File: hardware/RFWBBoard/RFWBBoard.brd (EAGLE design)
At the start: 90 x 56 mm, 87 parts, among them IC1 24LC025ST, J1 CON-71742-2184-BOT, M1 MOUNT-HOLE3.3, M2 MOUNT-HOLE3.3, M3 MOUNT-HOLE3.3, M4 MOUNT-HOLE3.3, U1 MAX2830IPC-7351, U2 LDB212G4010C-001, U3 LDB212G4010C-001, U4 AD8132MSOP8, U5 AD8132MSOP8, U6 AD8132MSOP8, U7 AD8132MSOP8, X1 LTI-SASF54GT, X2 LTI-SASF54GT, X4 LTI-SASF54GT, X5 LTI-SASF54GT, X6 LTI-SASF54GT, X7 LTI-SASF54GT

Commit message: - Schematic updated - Info text updated on PCB back - 84 pin component changed in library
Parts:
- J1: value CON-71742-2184-BOT -> CON-71742-3003-BOT
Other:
- board text added: "Radio Front-End Board Rev A"
- board text removed: "Radio Front-End Board"
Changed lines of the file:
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@@
 <grid distance="1" unitdist="mm" unit="mm" style="dots" multiple="1" display="yes" altdistance="0.05" altunitdist="mm" altunit="mm"/>
 <layers>
-<layer number="1" name="Top" color="4" fill="1" visible="no" active="yes"/>
+<layer number="1" name="Top" color="4" fill="1" visible="yes" active="yes"/>
 <layer number="2" name="Route2" color="14" fill="1" visible="no" active="yes"/>
 <layer number="3" name="Route3" color="4" fill="1" visible="no" active="yes"/>
 <layer number="14" name="Route14" color="1" fill="6" visible="no" active="no"/>
 <layer number="15" name="Route15" color="4" fill="6" visible="no" active="no"/>
-<layer number="16" name="Bottom" color="14" fill="1" visible="no" active="yes"/>
+<layer number="16" name="Bottom" color="14" fill="1" visible="yes" active="yes"/>
 <layer number="17" name="Pads" color="2" fill="1" visible="yes" active="yes"/>
-<layer number="18" name="Vias" color="2" fill="1" visible="no" active="yes"/>
+<layer number="18" name="Vias" color="2" fill="1" visible="yes" active="yes"/>
 <layer number="19" name="Unrouted" color="6" fill="1" visible="yes" active="yes"/>
 <layer number="20" name="Dimension" color="15" fill="1" visible="yes" active="yes"/>
@@
 <wire x1="70" y1="19" x2="70" y2="36" width="0.2032" layer="22"/>
 <wire x1="70" y1="36" x2="20" y2="36" width="0.2032" layer="22"/>
-<text x="61" y="33" size="1.778" layer="22" font="vector" rot="MR0">Radio Front-End Board</text>
+<text x="66" y="33" size="1.778" layer="22" font="vector" rot="MR0">Radio Front-End Board Rev A</text>
 <text x="69" y="30" size="1.27" layer="22" font="vector" rot="MR0">7.5-18 MHz wide 2.4-2.5 GHz/Baseband module</text>
 <text x="57.75" y="27.75" size="1.27" layer="22" font="vector" rot="MR0">for the Marmote platform</text>
@@
 <element name="M3" library="RFWBBoard" package="3,3" value="MOUNT-HOLE3.3" x="5" y="5" locked="yes"/>
 <element name="M4" library="RFWBBoard" package="3,3" value="MOUNT-HOLE3.3" x="85" y="5" locked="yes"/>
-<element name="J1" library="RFWBBoard" package="71742-3003-BOT" value="CON-71742-2184-BOT" x="45" y="7" smashed="yes" rot="MR180">
-<attribute name="DIGI-KEY#" value="WM3499CT-ND" x="45" y="7" size="1.778" layer="28" rot="MR180" display="off"/>
-<attribute name="MATED-STACKING-HEIGHT" value="13mm, 15mm" x="45" y="7" size="1.778" layer="28" rot="MR180" display="off"/>
-<attribute name="MF" value="Molex" x="45" y="7" size="1.778" layer="28" rot="MR180" display="off"/>
-<attribute name="MPN" value="71742-3003" x="45" y="7" size="1.778" layer="28" rot="MR180" display="off"/>
+<element name="J1" library="RFWBBoard" package="71742-3003-BOT" value="CON-71742-3003-BOT" x="45" y="7" smashed="yes" rot="MR180">
 <attribute name="NAME" x="21.7" y="11.65" size="1.27" layer="26" font="vector" rot="MR180"/>
 <attribute name="VALUE" x="45" y="11" size="0.4064" layer="28" rot="MR180"/>

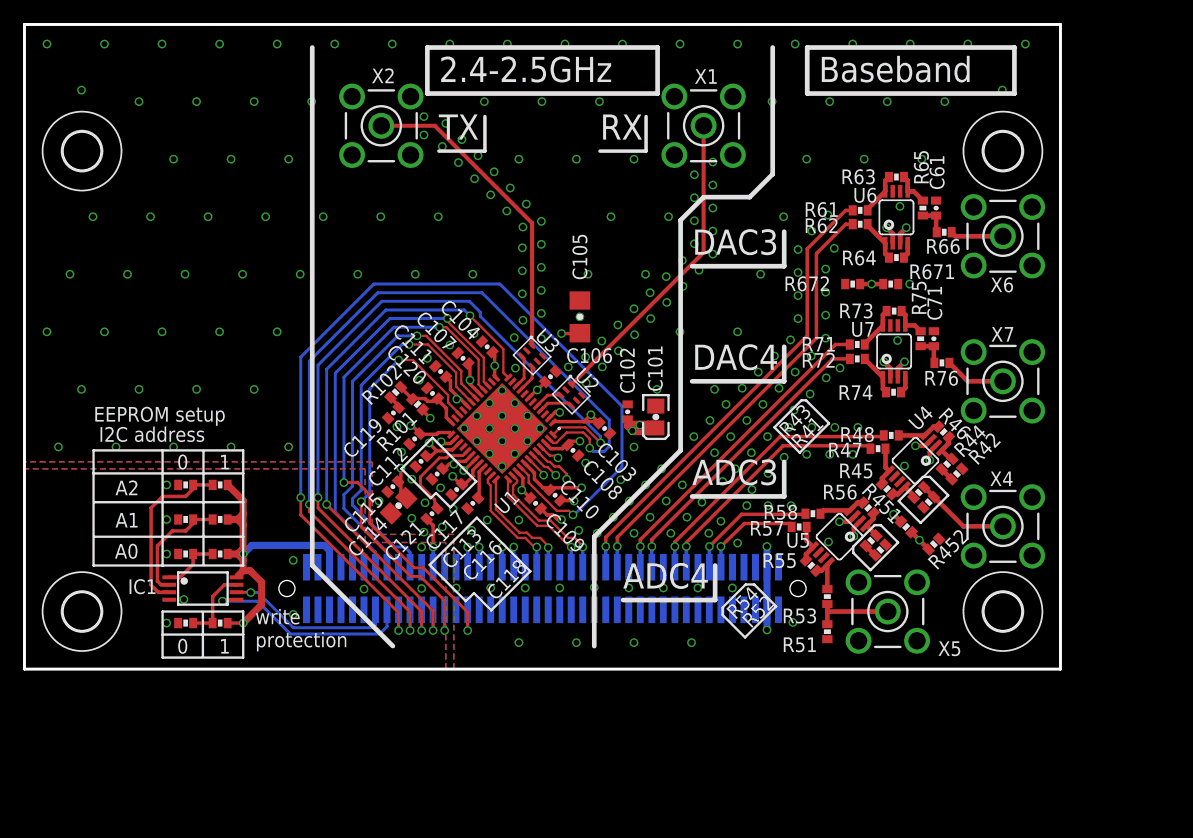
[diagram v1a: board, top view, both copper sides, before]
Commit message: - Pull-up resistors for I2C lines
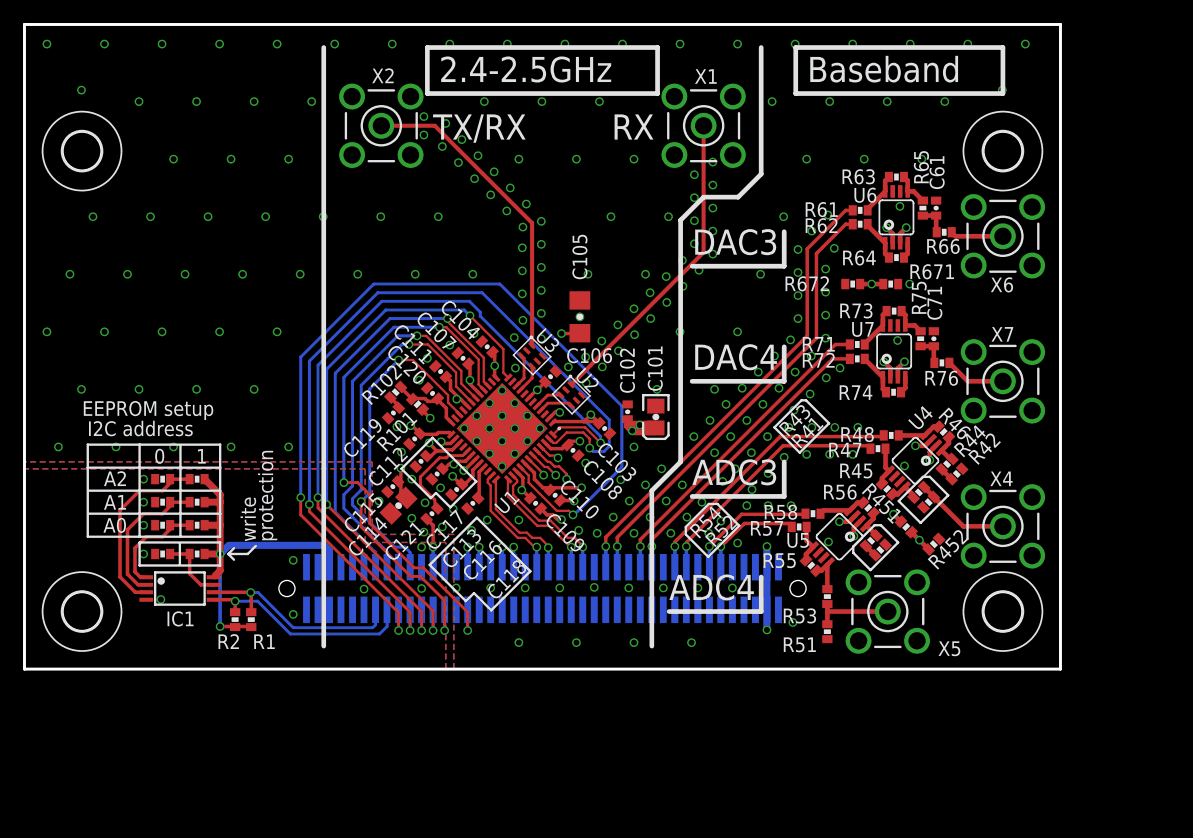
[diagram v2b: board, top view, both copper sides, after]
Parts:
- added R1, R2: 4.7k, RFWBBoard:R0402
- moved RWP0 6.32 mm to (12.0, 10.0)
- moved RWP1 6.32 mm to (15.0, 10.0)
- moved RA00 3.20 mm to (12.0, 12.5)
- moved RA01 3.20 mm to (15.0, 12.5)
- moved RA10 2.50 mm to (12.0, 14.5)
- moved RA11 2.50 mm to (15.0, 14.5)
- moved RA20 2.06 mm to (12.0, 16.5)
- moved RA21 2.06 mm to (15.0, 16.5)
- moved IC1 2.00 mm to (13.5, 7.00)
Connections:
- net D3V3: now also R1.2, R2.2
- net I2C1_SCL: now also R1.1
- net I2C1_SDA: now also R2.1
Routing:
- net A0: track 5.14 -> 9.01 mm
- net I2C1_SCL: track 14.8 -> 18.5 mm
- net D3V3: track 30.2 -> 33.7 mm
- net A1: track 10.2 -> 12.5 mm
- net A2: track 14.9 -> 16.0 mm
- net WP: track 6.60 -> 5.88 mm
- net I2C1_SDA: track 18.5 -> 19.0 mm
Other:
- board text added: "TX/RX"
- board text removed: "TX"

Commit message: - R and C footprints updated from Main Board project - 2.4 GHz and base-band ground part separated with gap - Board layers 4 -> 6 - Interface connector updated
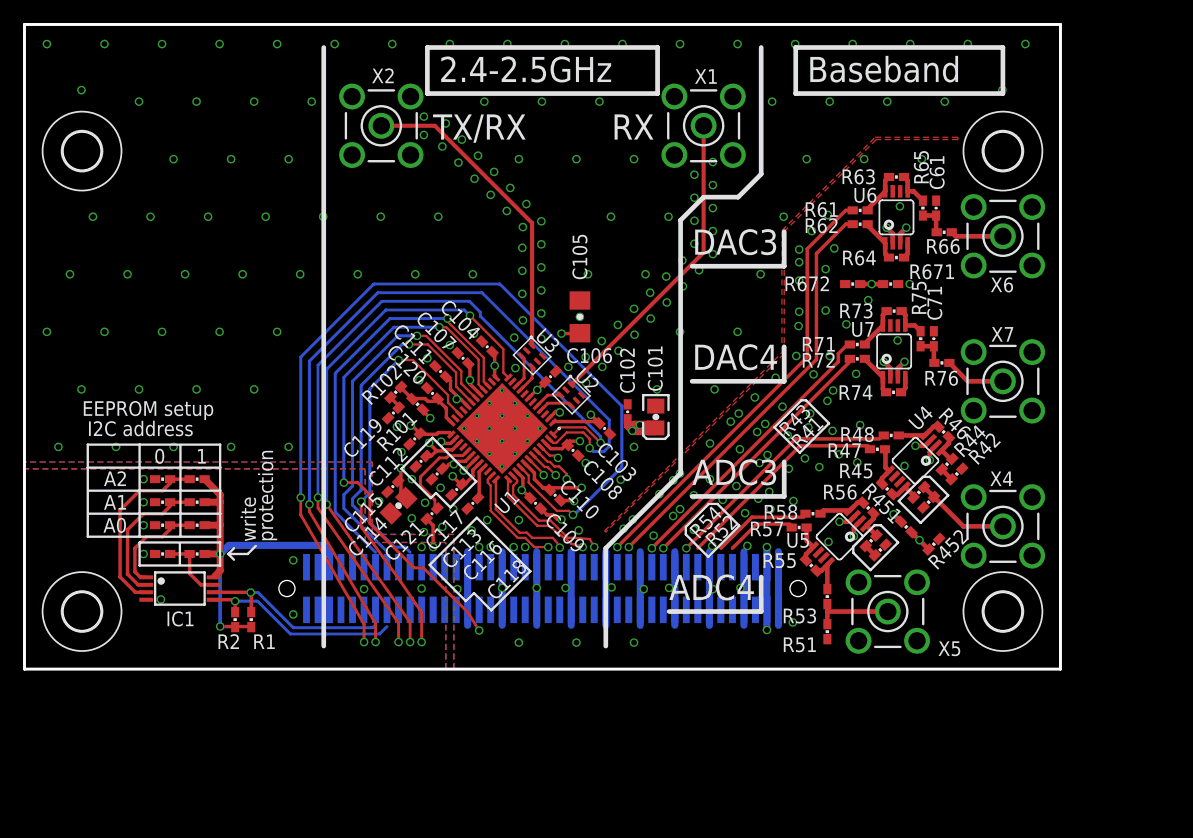
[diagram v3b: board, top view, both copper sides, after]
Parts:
- moved R47 0.07 mm to (74.1, 19.1)
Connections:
- net SPI1_MOSI renamed DIN
- removed net ADCHP1: J1.31
- removed net ADCHP3: J1.55
- removed net ADCSF1: J1.29, U1.16
- removed net ADCSF2: J1.35
- removed net ADCSF3: J1.53
- removed net ADCSF4: J1.59
- removed net ARESERVED: J1.77, J1.78
- removed net DACHP1: J1.43
- removed net DACHP2: J1.49
- removed net DACHP3: J1.67
- removed net DACHP4: J1.73
- removed net DACSF1: J1.41
- removed net DACSF2: J1.47
- removed net DACSF3: J1.65
- removed net DACSF4: J1.71
- removed net DRESERVED: J1.10, J1.9
- removed net GPIO1: J1.17, U1.40
- removed net GPIO2: J1.19, U1.47
- removed net GPIO3: J1.21, U1.48
- removed net GPIO4: J1.23, U1.12
- removed net GPIO5: J1.25, U1.22
- removed net I2C1_SCL: IC1.6, J1.13, R1.1
- removed net I2C1_SDA: IC1.5, J1.15, R2.1
- removed net SPI1_NSS: J1.14, U1.15
- removed net SPI1_SCK: J1.16, U1.18
- new net !CS: J1.24, U1.15
- new net !SHDN: J1.19, U1.12
- new net ANTSEL: J1.13, U1.47
- new net I2C_SCL: IC1.6, J1.26, R1.1
- new net I2C_SDA: IC1.5, J1.28, R2.1
- new net LD: J1.21, U1.22
- new net RSSI: J1.31, U1.16
- new net RXHP: J1.11, U1.40
- new net RXTX: J1.17, U1.48
- new net SCLK: J1.18, U1.18
- net ADC1+: now also J1.46; no longer J1.44
- net ADC1-: now also J1.44; no longer J1.42
- net ADC2+: now also J1.52; no longer J1.50
- net ADC2-: now also J1.50; no longer J1.48
- net ADC3+: now also J1.70; no longer J1.68
- net ADC3-: now also J1.68; no longer J1.66
- net ADC4+: now also J1.76; no longer J1.74
- net ADC4-: now also J1.74; no longer J1.72
- net AGND: now also J1.29, J1.30, J1.35, J1.36, J1.41, J1.42, J1.47, J1.48, J1.53, J1.54, J1.59, J1.60, J1.65, J1.66, J1.71, J1.72, J1.77, J1.78; no longer J1.27, J1.28, J1.33, J1.34, J1.37, J1.39, J1.40, J1.45, J1.46, J1.51, J1.52, J1.57, J1.58, J1.61, J1.63, J1.64, J1.69, J1.70, J1.75, J1.76
- net CLK1: now also J1.12; no longer J1.24
- net CLK2: now also J1.14; no longer J1.26
- net DAC1+: now also J1.34; no longer J1.32
- net DAC1-: now also J1.32; no longer J1.30
- net DAC2+: now also J1.40; no longer J1.38
- net DAC2-: now also J1.38; no longer J1.36
- net DAC3+: now also J1.58; no longer J1.56
- net DAC3-: now also J1.56; no longer J1.54
- net DAC4+: now also J1.64; no longer J1.62
- net DAC4-: now also J1.62; no longer J1.60
- net DGND: now also J1.10, J1.15, J1.16, J1.9; no longer J1.11, J1.12, J1.22
- net SPI1_MISO: now also J1.22; no longer J1.18
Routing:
- net GPIO1: track 81.9 -> 0.00 mm, vias 3 -> 0
- net RXHP: track 0.00 -> 79.1 mm, vias 0 -> 3
- net GPIO2: track 71.3 -> 0.00 mm, vias 3 -> 0
- net ANTSEL: track 0.00 -> 68.5 mm, vias 0 -> 3
- net GPIO3: track 66.0 -> 0.00 mm, vias 3 -> 0
- net AGND: track 7.03 -> 71.0 mm, vias 252 -> 249
- net RXTX: track 0.00 -> 63.7 mm, vias 0 -> 3
- net GPIO4: track 49.9 -> 0.00 mm, vias 3 -> 0
- net !SHDN: track 0.00 -> 47.6 mm, vias 0 -> 3
- net ADCSF1: track 46.9 -> 0.00 mm, vias 3 -> 0
- net RSSI: track 0.00 -> 45.4 mm, vias 0 -> 3
- net GPIO5: track 37.5 -> 0.00 mm, vias 3 -> 0
- net SPI1_NSS: track 37.3 -> 0.00 mm, vias 1 -> 0
- net !CS: track 0.00 -> 36.0 mm, vias 0 -> 1
- net LD: track 0.00 -> 34.9 mm, vias 0 -> 3
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- added copper zone on layer 1, net N$35

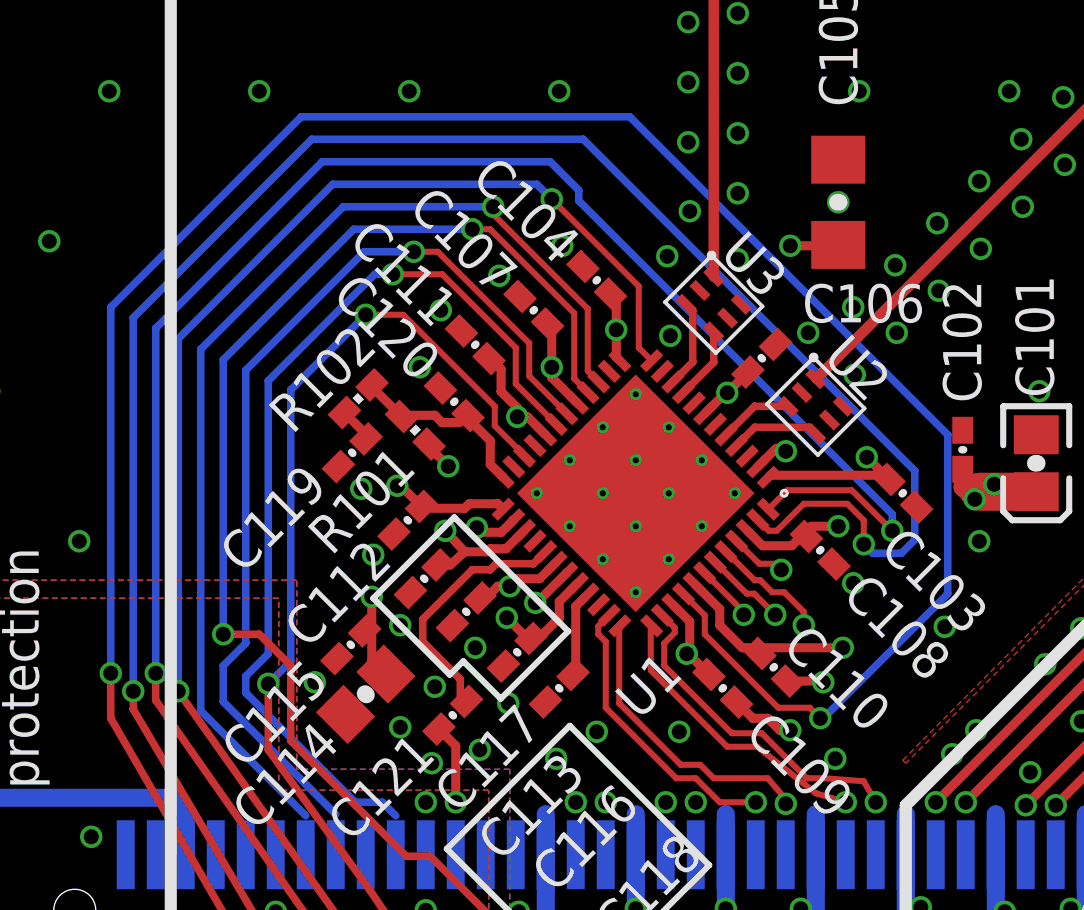
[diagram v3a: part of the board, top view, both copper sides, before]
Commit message: - Layout update - Interface update (RSSI -> SF_ADC6)
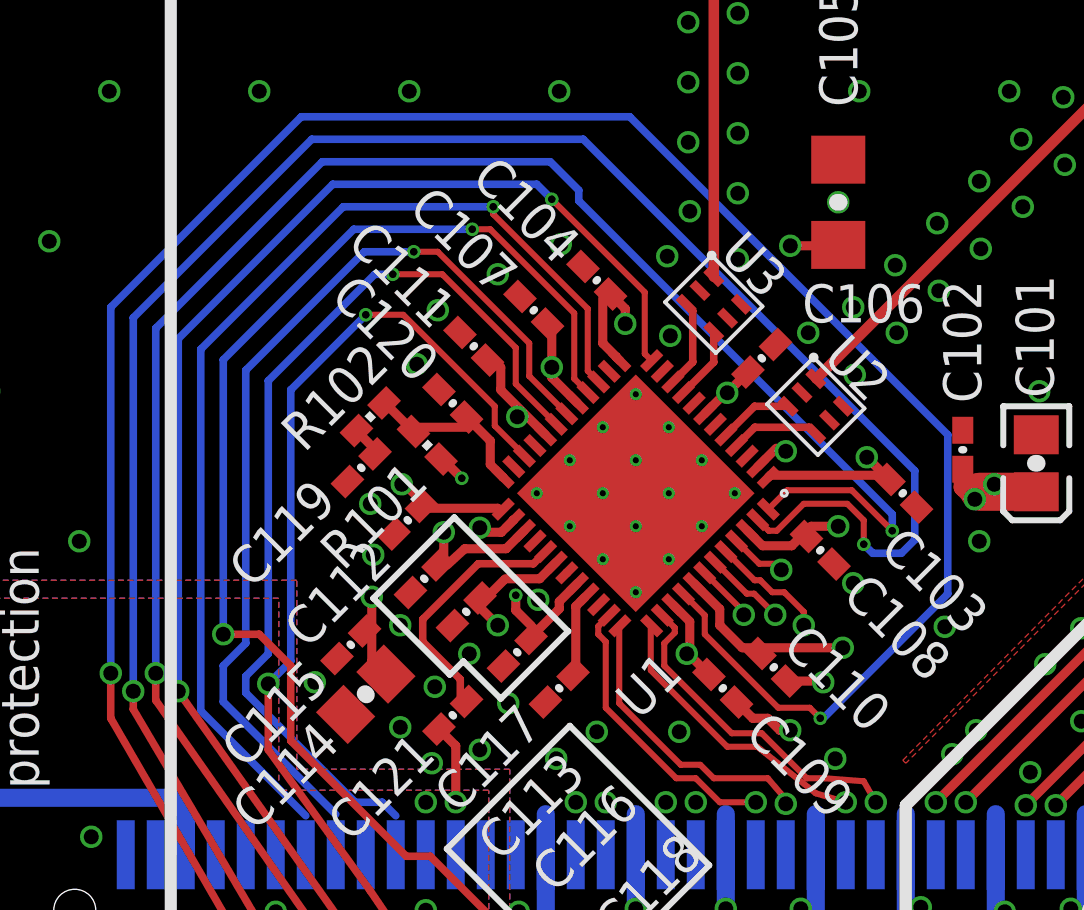
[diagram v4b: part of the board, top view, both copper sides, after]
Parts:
- moved R102 0.72 mm to (32.6, 23.4)
- moved R101 0.64 mm to (34.5, 22.5)
- moved C119 0.58 mm to (32.4, 21.8)
- moved C120 0.07 mm to (35.4, 23.9)
- moved C111 0.07 mm to (36.1, 25.8)
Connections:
- net RSSI: now also J1.39; no longer J1.31
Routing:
- net N$5: track 10.7 -> 9.07 mm
- net DAC1-: track 12.5 -> 10.9 mm
- net A3V3: track 191.2 -> 192.7 mm
- net AGND: track 71.0 -> 69.6 mm
- net DAC2-: track 13.1 -> 11.7 mm
- net DAC2+: track 13.4 -> 12.3 mm
